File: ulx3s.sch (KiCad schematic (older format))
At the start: 18 parts, among them IC1 MT48LC16M4A2P, U1 LFE5U-25F-6BG381C, U2 ESP-12E

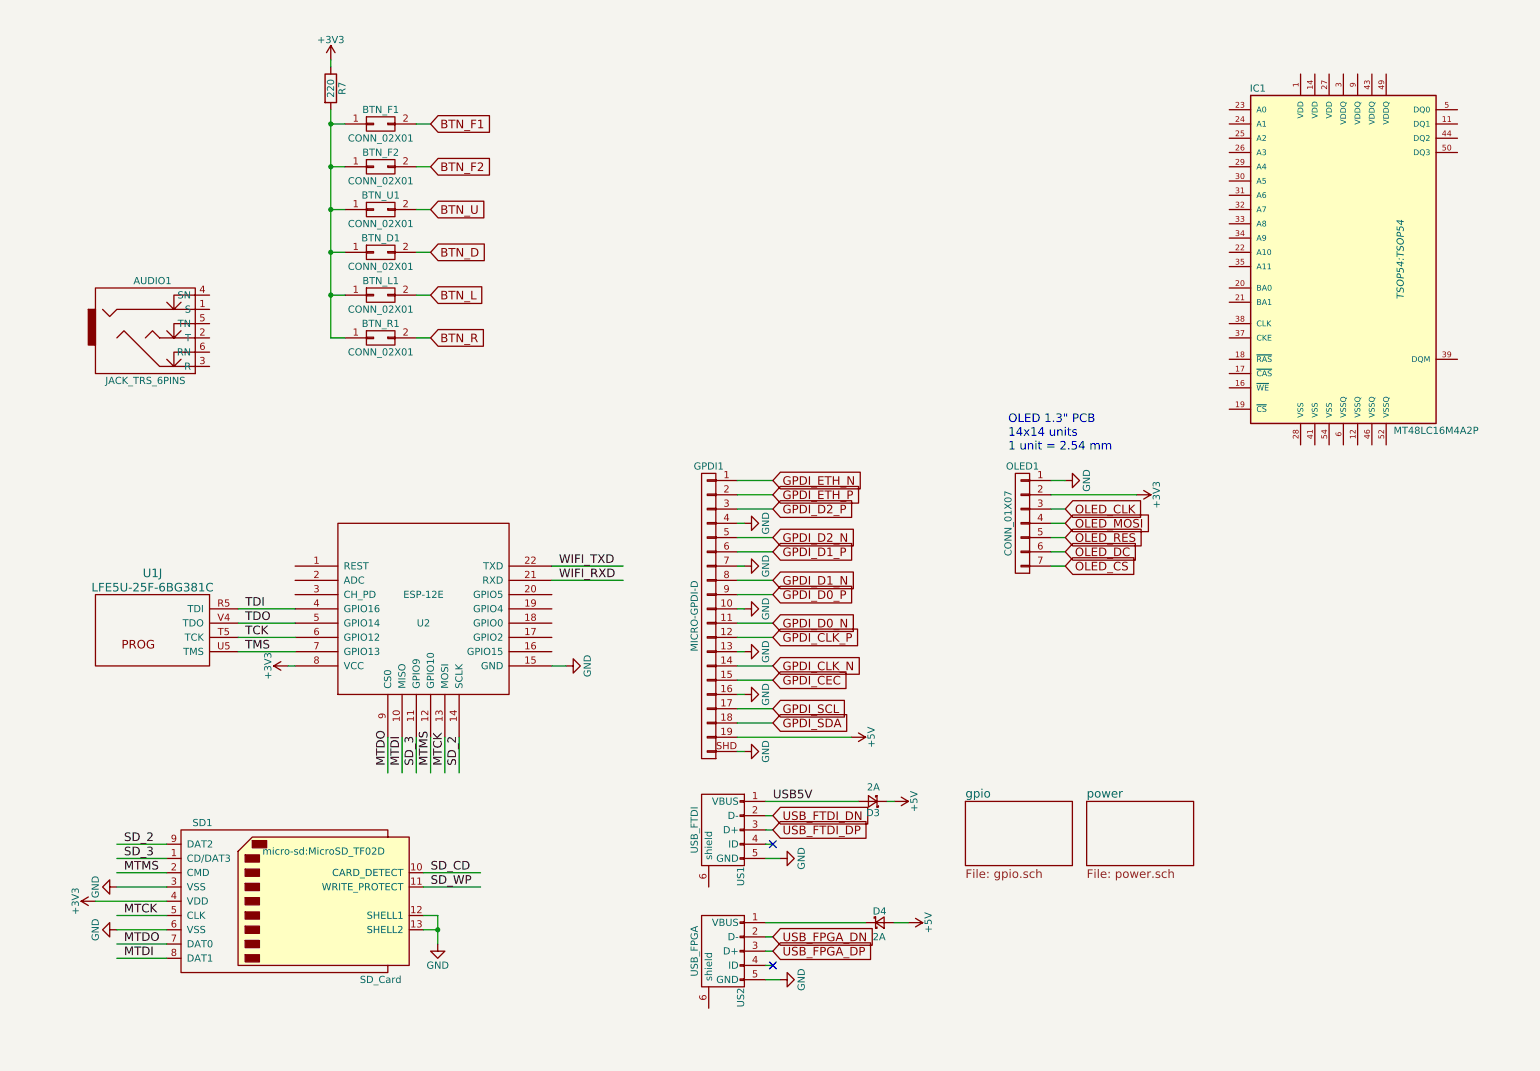
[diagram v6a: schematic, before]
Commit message: Moving LEDs, OLED and buttons to "blinkey" sheet
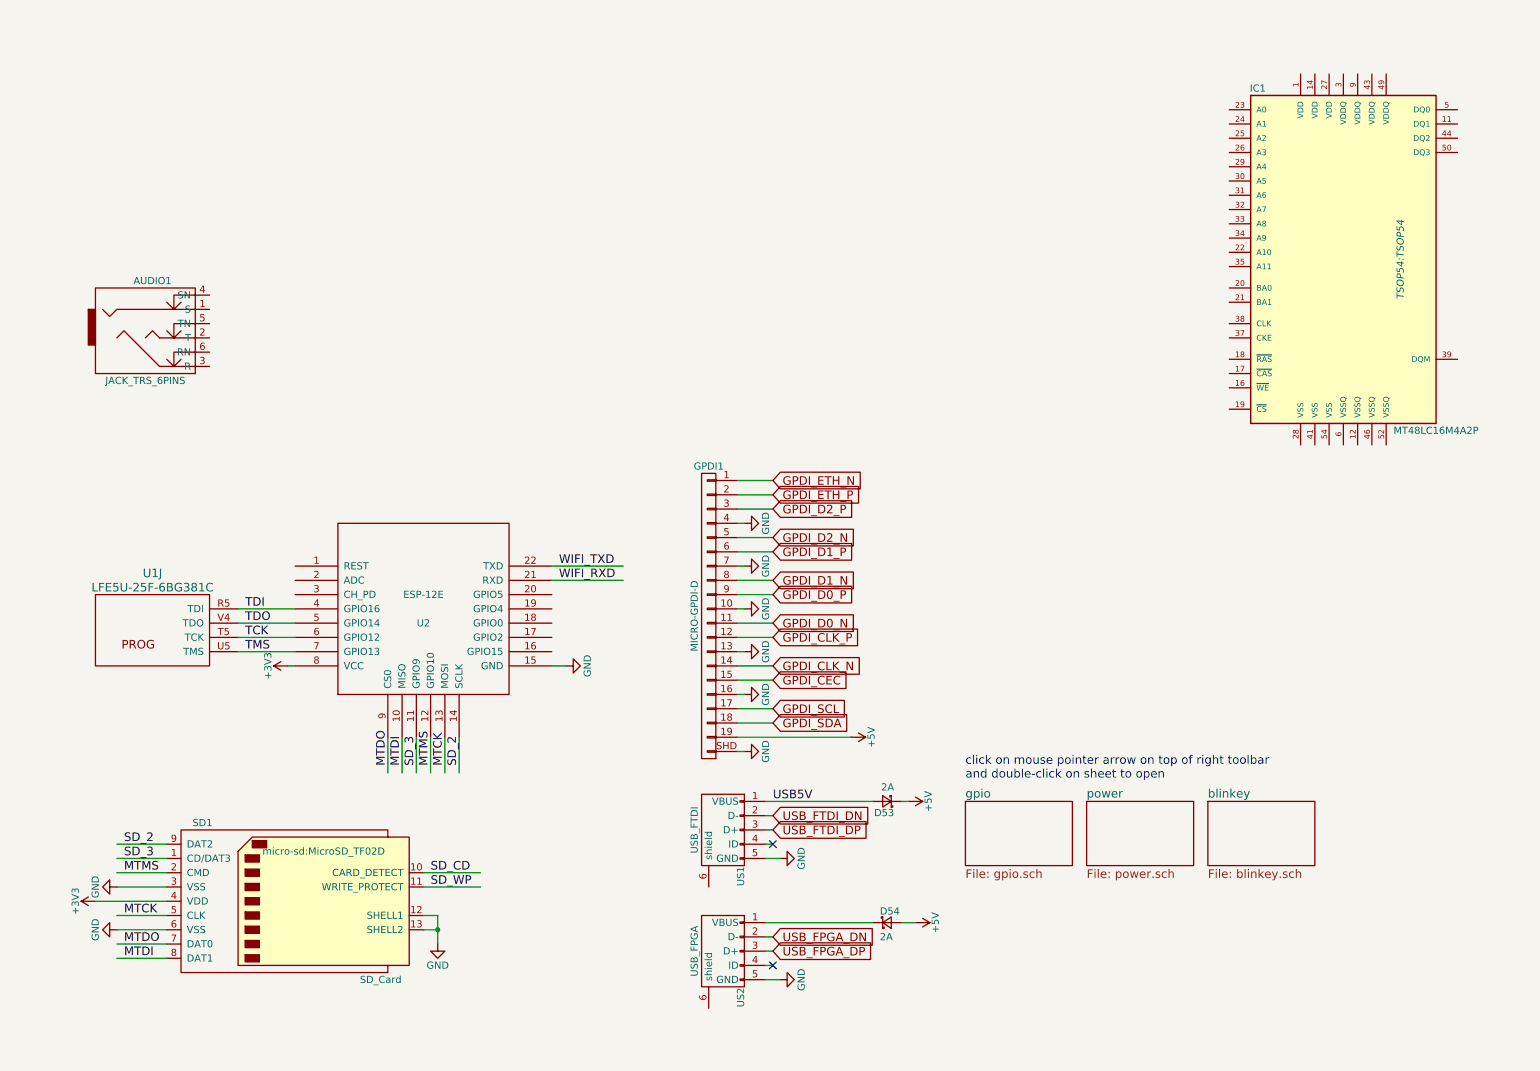
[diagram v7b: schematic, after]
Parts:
- removed BTN_D1, BTN_F1, BTN_F2, BTN_L1, BTN_R1, BTN_U1: CONN_02X01, Buttons_Switches_SMD:SW_SPST_SKQG, symbol CONN_02X01
- removed OLED1: CONN_01X07, Socket_Strips:Socket_Strip_Straight_1x07, symbol CONN_01X07
- removed R7: 220, Resistors_SMD:R_0805_HandSoldering, symbol R
- renumbered D3 to D53, D4 to D54
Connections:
- net labels removed: BTN_D, BTN_F1, BTN_F2, BTN_L, BTN_R, BTN_U, OLED_CLK, OLED_CS, OLED_DC, OLED_MOSI, OLED_RES
- wire segments 81 -> 60
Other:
- note added: "click on mouse pointer arrow on top of right toolbar\nand double-click on sheet to open"
- note removed: "OLED 1.3" PCB \n14x14 units\n1 unit = 2.54 mm"
- moved on the sheet: D53, D54

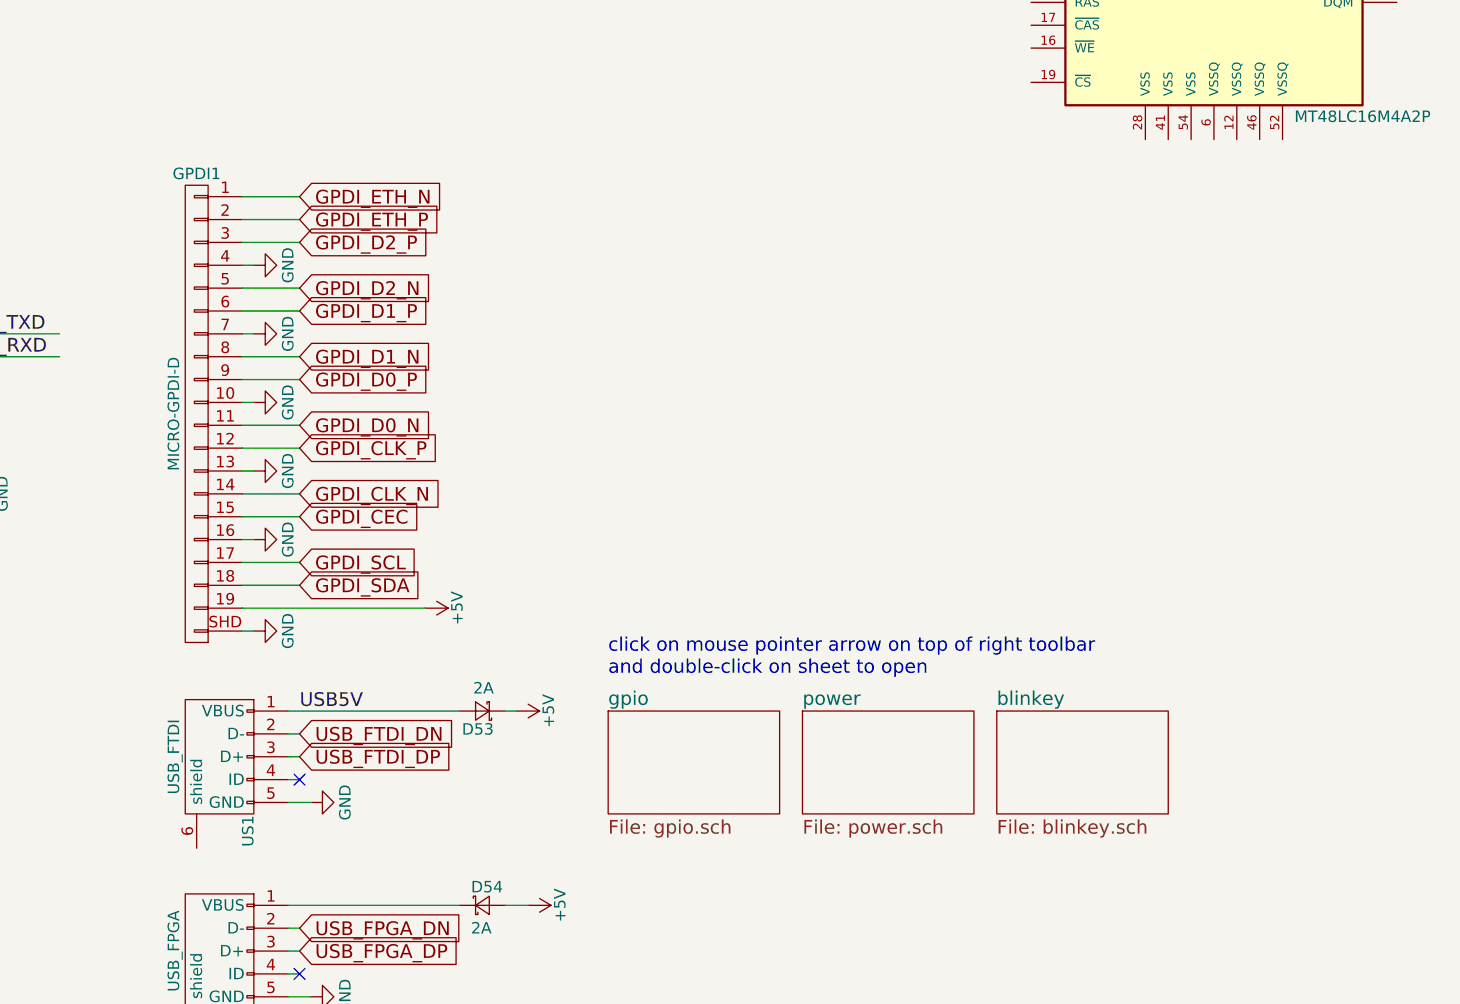
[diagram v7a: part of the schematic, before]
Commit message: GPDI to separate sheet
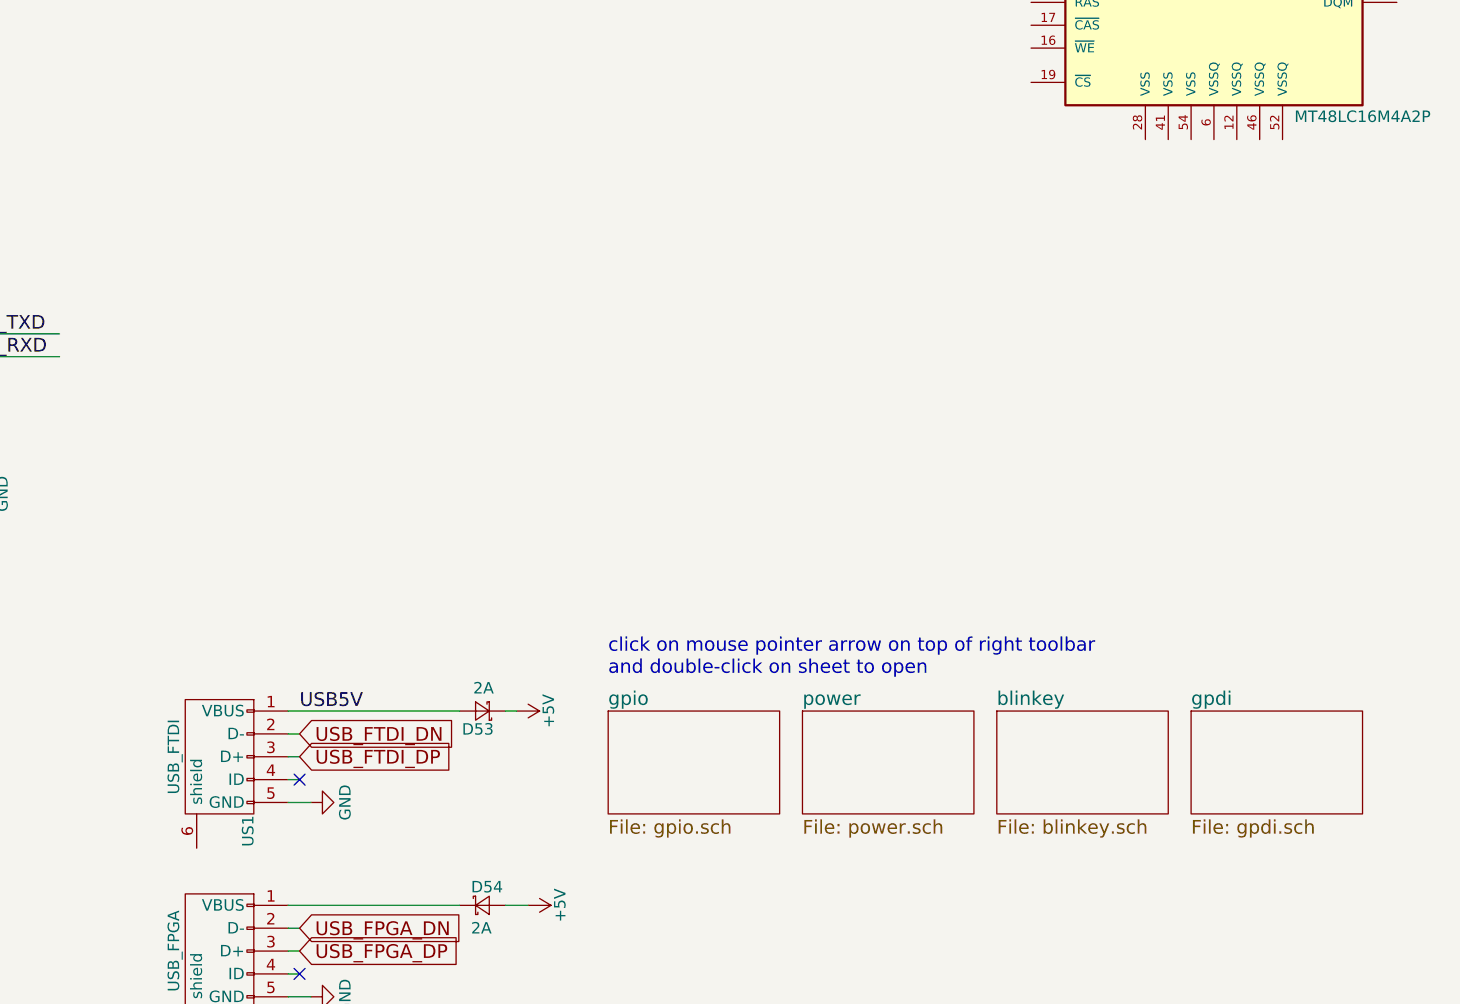
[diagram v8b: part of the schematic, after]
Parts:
- removed GPDI1: MICRO-GPDI-D, micro-hdmi-d:MICRO-HDMI-D, symbol MICRO-HDMI-D
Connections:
- net labels removed: GPDI_CEC, GPDI_CLK_N, GPDI_CLK_P, GPDI_D0_N, GPDI_D0_P, GPDI_D1_N, GPDI_D1_P, GPDI_D2_N, GPDI_D2_P, GPDI_ETH_N, GPDI_ETH_P, GPDI_SCL, GPDI_SDA
- wire segments 60 -> 40
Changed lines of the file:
@@
 $Descr A4 11693 8268
 encoding utf-8
-Sheet 1 4
+Sheet 1 5
 Title "ULX3S"
 Date ""
@@
 	1    2300 6600
 	1    0    0    -1
-$EndComp
-$Comp
-L MICRO-HDMI-D GPDI1
-U 1 1 56ACD5D4
-P 5200 4600
-F 0 "GPDI1" H 5200 5650 50  0000 C CNN
-F 1 "MICRO-GPDI-D" V 5300 4600 50  0000 C CNN
-F 2 "micro-hdmi-d:MICRO-HDMI-D" H 5200 4600 60  0001 C CNN
-F 3 "" H 5200 4600 60  0000 C CNN
-	1    5200 4600
-	-1   0    0    -1
 $EndComp
 $Comp
@@
 	0    -1   -1   0
 $EndComp
-Wire Wire Line
-	5400 3650 5650 3650
-Wire Wire Line
-	5400 3750 5650 3750
-Wire Wire Line
-	5400 3850 5650 3850
-Wire Wire Line
-	5400 5150 5450 5150
-Wire Wire Line
-	5400 3950 5450 3950
-Wire Wire Line
-	5400 4050 5650 4050
-Wire Wire Line
-	5400 4150 5650 4150
-Wire Wire Line
-	5400 4250 5450 4250
-Wire Wire Line
-	5400 4350 5650 4350
-Wire Wire Line
-	5400 4450 5650 4450
-Wire Wire Line
-	5400 4550 5450 4550
-Wire Wire Line
-	5400 4650 5650 4650
-Wire Wire Line
-	5400 4750 5650 4750
-Wire Wire Line
-	5400 4850 5450 4850
-Wire Wire Line
-	5400 4950 5650 4950
-Wire Wire Line
-	5400 5050 5650 5050
-Wire Wire Line
-	5400 5250 5650 5250
-Wire Wire Line
-	5400 5450 6200 5450
-Wire Wire Line
-	5400 5350 5650 5350
-Wire Wire Line
-	5400 5550 5450 5550
-$Comp
-L GND #PWR06
-U 1 1 58D544FB
-P 5450 5550
-F 0 "#PWR06" H 5450 5300 50  0001 C CNN
-F 1 "GND" H 5450 5400 50  0000 C CNN
-F 2 "" H 5450 5550 60  0000 C CNN
-F 3 "" H 5450 5550 60  0000 C CNN
-	1    5450 5550
-	0    -1   -1   0
-$EndComp
-$Comp
-L GND #PWR07
-U 1 1 58D5464C
-P 5450 5150
-F 0 "#PWR07" H 5450 4900 50  0001 C CNN
-F 1 "GND" H 5450 5000 50  0000 C CNN
-F 2 "" H 5450 5150 60  0000 C CNN
-F 3 "" H 5450 5150 60  0000 C CNN
-	1    5450 5150
-	0    -1   -1   0
-$EndComp
-$Comp
-L GND #PWR08
-U 1 1 58D54683
-P 5450 4850
-F 0 "#PWR08" H 5450 4600 50  0001 C CNN
-F 1 "GND" H 5450 4700 50  0000 C CNN
-F 2 "" H 5450 4850 60  0000 C CNN
-F 3 "" H 5450 4850 60  0000 C CNN
-	1    5450 4850
-	0    -1   -1   0
-$EndComp
-$Comp
-L GND #PWR09
-U 1 1 58D54712
-P 5450 4550
-F 0 "#PWR09" H 5450 4300 50  0001 C CNN
-F 1 "GND" H 5450 4400 50  0000 C CNN
-F 2 "" H 5450 4550 60  0000 C CNN
-F 3 "" H 5450 4550 60  0000 C CNN
-	1    5450 4550
-	0    -1   -1   0
-$EndComp
-$Comp
-L GND #PWR010
-U 1 1 58D54749
-P 5450 4250
-F 0 "#PWR010" H 5450 4000 50  0001 C CNN
-F 1 "GND" H 5450 4100 50  0000 C CNN
-F 2 "" H 5450 4250 60  0000 C CNN
-F 3 "" H 5450 4250 60  0000 C CNN
-	1    5450 4250
-	0    -1   -1   0
-$EndComp
-$Comp
-L GND #PWR011
-U 1 1 58D547C2
-P 5450 3950
-F 0 "#PWR011" H 5450 3700 50  0001 C CNN
-F 1 "GND" H 5450 3800 50  0000 C CNN
-F 2 "" H 5450 3950 60  0000 C CNN
-F 3 "" H 5450 3950 60  0000 C CNN
-	1    5450 3950
-	0    -1   -1   0
-$EndComp
 $Sheet
 S 7850 5900 750  450
@@
 	1050 6800 1400 6800
 $Comp
-L GND #PWR012
+L GND #PWR06
 U 1 1 58D58197
 P 1050 6500
-F 0 "#PWR012" H 1050 6250 50  0001 C CNN
+F 0 "#PWR06" H 1050 6250 50  0001 C CNN
 F 1 "GND" H 1050 6350 50  0000 C CNN
 F 2 "" H 1050 6500 50  0000 C CNN
@@
 $EndComp
 $Comp
-L GND #PWR013
+L GND #PWR07
 U 1 1 58D581BF
 P 1050 6800
-F 0 "#PWR013" H 1050 6550 50  0001 C CNN
+F 0 "#PWR07" H 1050 6550 50  0001 C CNN
 F 1 "GND" H 1050 6650 50  0000 C CNN
 F 2 "" H 1050 6800 50  0000 C CNN
@@
 SD_WP
 $Comp
-L GND #PWR014
+L GND #PWR08
 U 1 1 58D58733
 P 3300 6900
-F 0 "#PWR014" H 3300 6650 50  0001 C CNN
+F 0 "#PWR08" H 3300 6650 50  0001 C CNN
 F 1 "GND" H 3300 6750 50  0000 C CNN
 F 2 "" H 3300 6900 50  0000 C CNN
@@
 Connection ~ 3300 6800
 $Comp
-L +3V3 #PWR015
+L +3V3 #PWR09
 U 1 1 58D5F08C
 P 2250 4950
-F 0 "#PWR015" H 2250 4800 50  0001 C CNN
+F 0 "#PWR09" H 2250 4800 50  0001 C CNN
 F 1 "+3V3" H 2250 5090 50  0000 C CNN
 F 2 "" H 2250 4950 50  0000 C CNN
@@
 $EndComp
 $Comp
-L +3V3 #PWR016
+L +3V3 #PWR010
 U 1 1 58D5F123
 P 900 6600
-F 0 "#PWR016" H 900 6450 50  0001 C CNN
+F 0 "#PWR010" H 900 6450 50  0001 C CNN
 F 1 "+3V3" H 900 6740 50  0000 C CNN
 F 2 "" H 900 6600 50  0000 C CNN
@@
 	0    -1   -1   0
 $EndComp
-$Comp
-L +5V #PWR017
-U 1 1 58D5F259
-P 6200 5450
-F 0 "#PWR017" H 6200 5300 50  0001 C CNN
-F 1 "+5V" H 6200 5590 50  0000 C CNN
-F 2 "" H 6200 5450 50  0000 C CNN
-F 3 "" H 6200 5450 50  0000 C CNN
-	1    6200 5450
-	0    1    1    0
-$EndComp
-Text GLabel 5650 3650 2    60   Input ~ 0
-GPDI_ETH_N
-Text GLabel 5650 3750 2    60   Input ~ 0
-GPDI_ETH_P
-Text GLabel 5650 3850 2    60   Input ~ 0
-GPDI_D2_P
-Text GLabel 5650 4050 2    60   Input ~ 0
-GPDI_D2_N
-Text GLabel 5650 4150 2    60   Input ~ 0
-GPDI_D1_P
-Text GLabel 5650 4350 2    60   Input ~ 0
-GPDI_D1_N
-Text GLabel 5650 4450 2    60   Input ~ 0
-GPDI_D0_P
-Text GLabel 5650 4650 2    60   Input ~ 0
-GPDI_D0_N
-Text GLabel 5650 4750 2    60   Input ~ 0
-GPDI_CLK_P
-Text GLabel 5650 4950 2    60   Input ~ 0
-GPDI_CLK_N
-Text GLabel 5650 5050 2    60   Input ~ 0
-GPDI_CEC
-Text GLabel 5650 5250 2    60   Input ~ 0
-GPDI_SCL
-Text GLabel 5650 5350 2    60   Input ~ 0
-GPDI_SDA
 Text GLabel 5650 6000 2    60   Input ~ 0
 USB_FTDI_DN
@@
 Text Notes 7000 5750 0    60   ~ 0
 click on mouse pointer arrow on top of right toolbar\nand double-click on sheet to open
+$Sheet
+S 9550 5900 750  450
+U 58D686D9
+F0 "gpdi" 60
+F1 "gpdi.sch" 60
+$EndSheet
 $EndSCHEMATC
